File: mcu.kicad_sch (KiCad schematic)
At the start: 1 part, among them IC5 STM32G030K6T6

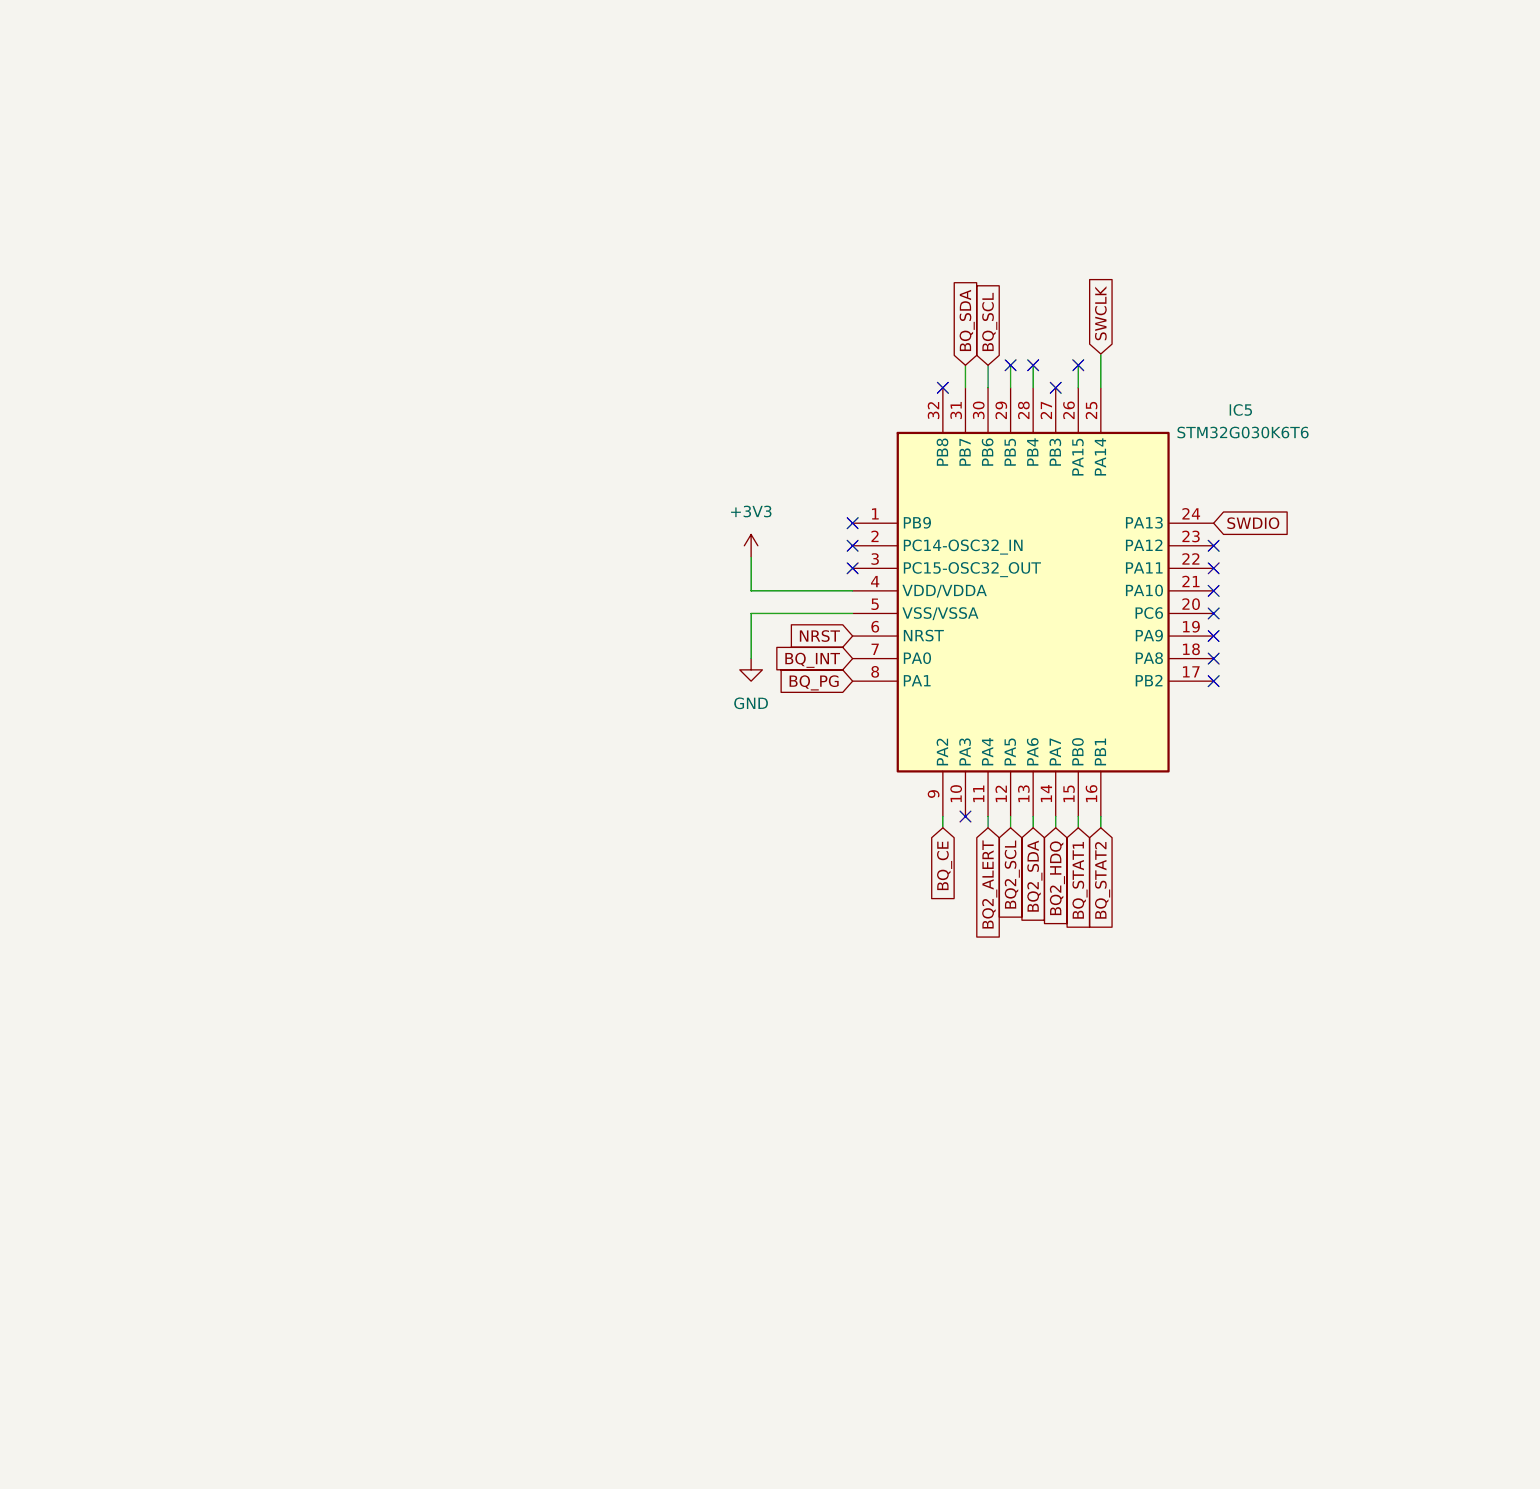
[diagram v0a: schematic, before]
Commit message: Added Canbus+LEDs+New STM32
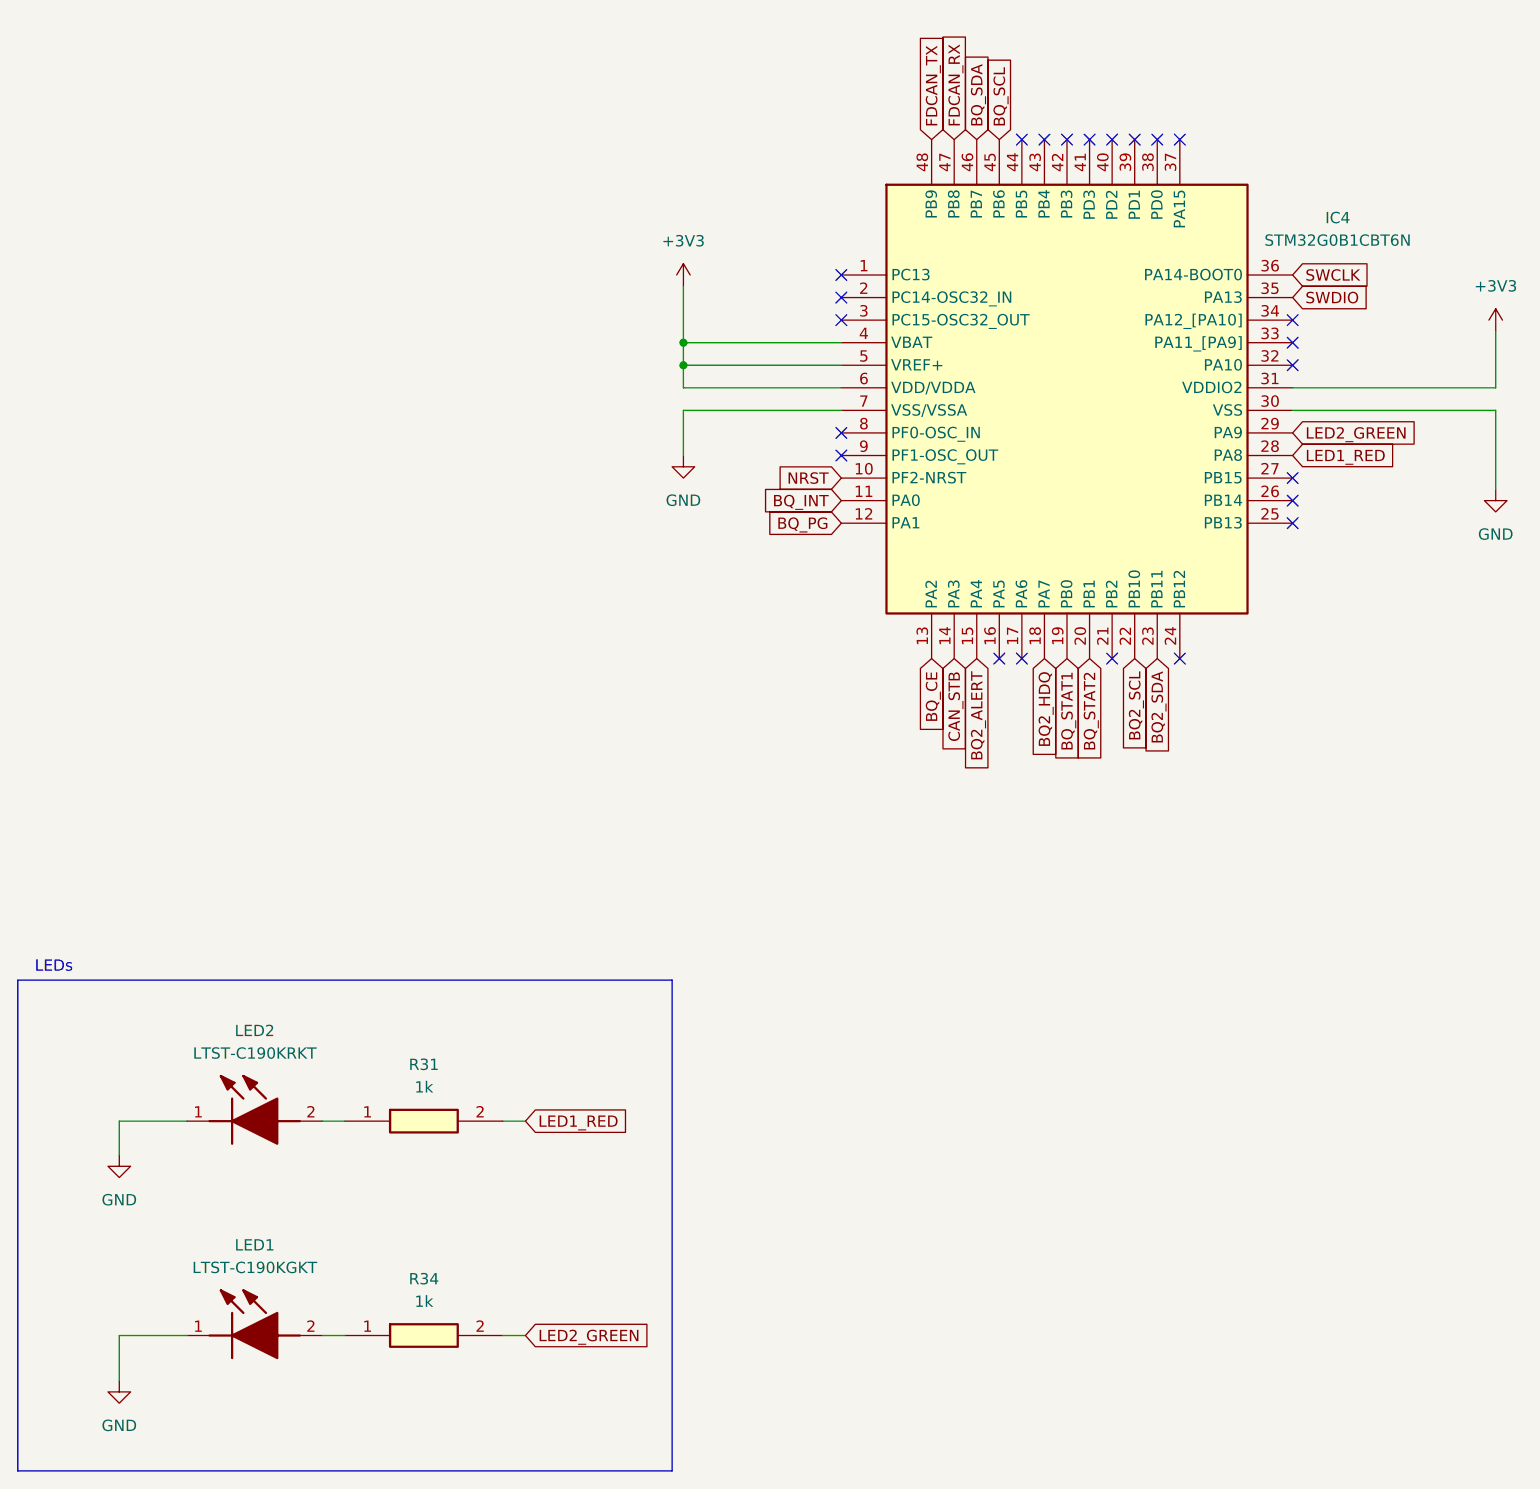
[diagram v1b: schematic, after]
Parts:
- removed IC5: STM32G030K6T6, STM32G030K6T6:QFP80P900X900X160-32N, symbol STM32G030K6T6:STM32G030K6T6
- added IC4: STM32G0B1CBT6N, STM32G0B1CBT6N:QFP50P900X900X160-48N, symbol STM32G0B1CBT6N:STM32G0B1CBT6N
- added LED1: LTST-C190KGKT, LTST-C190KGKT:LEDC1608X80N, symbol LTST-C190KGKT:LTST-C190KGKT
- added LED2: LTST-C190KRKT, LTST-C190KRKT:LEDC1608X80N, symbol LTST-C190KRKT:LTST-C190KRKT
- added R31, R34: 1k, RC0603FR-071KL:RESC1608X55N, symbol RC0603FR-071KL:RC0603FR-071KL
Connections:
- net +3V3: now also IC4.31 (VDDIO2), IC4.4 (VBAT), IC4.5 (VREF+), IC4.6 (VDD/VDDA)
- net BQ2_ALERT: now also IC4.15 (PA4)
- net BQ2_HDQ: now also IC4.18 (PA7)
- net BQ2_SCL: now also IC4.22 (PB10)
- net BQ2_SDA: now also IC4.23 (PB11)
- net BQ_CE: now also IC4.13 (PA2)
- net BQ_INT: now also IC4.11 (PA0)
- net BQ_PG: now also IC4.12 (PA1)
- net BQ_SCL: now also IC4.45 (PB6)
- net BQ_SDA: now also IC4.46 (PB7)
- net BQ_STAT1: now also IC4.19 (PB0)
- net BQ_STAT2: now also IC4.20 (PB1)
- net GND: now also IC4.30 (VSS), IC4.7 (VSS/VSSA), LED1.1 (K), LED2.1 (K)
- net NRST: now also IC4.10 (PF2-NRST)
- net SWCLK: now also IC4.36 (PA14-BOOT0)
- net SWDIO: now also IC4.35 (PA13)
- new net: LED2.2 (A), R31.1
- new net: LED1.2 (A), R34.1
- new net CAN_STB: IC4.14 (PA3)
- new net FDCAN_RX: IC4.47 (PB8)
- new net FDCAN_TX: IC4.48 (PB9)
- new net LED1_RED: IC4.28 (PA8), R31.2
- new net LED2_GREEN: IC4.29 (PA9), R34.2
- no-connect marks 16 -> 23
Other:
- note added: "LEDs"

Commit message: First Layout Try
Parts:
- added C14: 1uF, C2012X7R1H105K125AB:CAPC2012X145N, symbol C2012X7R1H105K125AB:C2012X7R1H105K125AB
- added C15, C27, C28: 0.1uF, CC0603KRX7R9BB104:CAPC1608X90N, symbol CC0603KRX7R9BB104:CC0603KRX7R9BB104
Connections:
- net +3V3: now also C14.1, C15.1, C27.1, C28.1
- net GND: now also C14.2, C15.2, C27.2, C28.2
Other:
- note added: "50V"
- note added: "Decoupling Capacitors"

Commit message: First Changes
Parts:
- removed C14: 1uF, C2012X7R1H105K125AB:CAPC2012X145N, symbol C2012X7R1H105K125AB:C2012X7R1H105K125AB
- added C14: 4.7uF, UMJ325AB7475KMHP:CAPC3225X280N, symbol UMJ325AB7475KMHP:UMJ325AB7475KMHP
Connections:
- net +3V3: now also C14.1
- net GND: now also C14.2
- net BQ2_SCLK: now reaches IC4.16 (PA5)
- net BQ2_MISO: now reaches IC4.17 (PA6)
- net BQ2_CS: now reaches IC4.24 (PB12)
- net BQ2_HDQ renamed BQ2_MOSI
- net BQ2_SCL: no longer names the net of IC4.22 (PB10)
- net BQ2_SDA: no longer names the net of IC4.23 (PB11)
- no-connect marks 23 -> 22
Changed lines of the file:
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@@
 	(text "50V"
 		(exclude_from_sim no)
-		(at 104.14 161.544 0)
+		(at 103.378 161.798 0)
 		(effects
 			(font
@@
 	)
 	(no_connect
-		(at 137.16 97.79)
+		(at 152.4 97.79)
 	)
 	(no_connect
@@
 	)
 	(no_connect
-		(at 134.62 97.79)
-	)
-	(no_connect
 		(at 149.86 39.37)
-	)
-	(no_connect
-		(at 154.94 97.79)
 	)
 	(no_connect
@@
 	(no_connect
 		(at 167.64 82.55)
+	)
+	(no_connect
+		(at 149.86 97.79)
 	)
 	(no_connect
@@
 		)
 	)
-	(global_label "BQ2_HDQ"
+	(global_label "BQ2_MOSI"
 		(shape input)
 		(at 139.7 97.79 270)
@@
 		)
 		(property "Intersheetrefs" "${INTERSHEET_REFS}"
-			(at 139.7 109.4838 90)
+			(at 139.7 110.149 90)
 			(effects
 				(font
@@
 		)
 	)
+	(global_label "BQ2_CS"
+		(shape input)
+		(at 154.94 97.79 270)
+		(fields_autoplaced yes)
+		(effects
+			(font
+				(size 1.27 1.27)
+			)
+			(justify right)
+		)
+		(property "Intersheetrefs" "${INTERSHEET_REFS}"
+			(at 154.94 108.0323 90)
+			(effects
+				(font
+					(size 1.27 1.27)
+				)
+				(justify right)
+				(hide yes)
+			)
+		)
+	)
 	(global_label "LED1_RED"
 		(shape input)
@@
 		)
 	)
+	(global_label "BQ2_SCLK"
+		(shape input)
+		(at 134.62 97.79 270)
+		(fields_autoplaced yes)
+		(effects
+			(font
+				(size 1.27 1.27)
+			)
+			(justify right)
+		)
+		(property "Intersheetrefs" "${INTERSHEET_REFS}"
+			(at 134.62 110.3304 90)
+			(effects
+				(font
+					(size 1.27 1.27)
+				)
+				(justify right)
+				(hide yes)
+			)
+		)
+	)
 	(global_label "SWCLK"
 		(shape input)
@@
 		)
 	)
-	(global_label "BQ2_SDA"
-		(shape input)
-		(at 152.4 97.79 270)
-		(fields_autoplaced yes)
-		(effects
-			(font
-				(size 1.27 1.27)
-			)
-			(justify right)
-		)
-		(property "Intersheetrefs" "${INTERSHEET_REFS}"
-			(at 152.4 109.1209 90)
-			(effects
-				(font
-					(size 1.27 1.27)
-				)
-				(justify right)
-				(hide yes)
-			)
-		)
-	)
 	(global_label "BQ_STAT2"
 		(shape input)
@@
 		)
 	)
-	(global_label "BQ2_SCL"
-		(shape input)
-		(at 149.86 97.79 270)
-		(fields_autoplaced yes)
-		(effects
-			(font
-				(size 1.27 1.27)
-			)
-			(justify right)
-		)
-		(property "Intersheetrefs" "${INTERSHEET_REFS}"
-			(at 149.86 109.0604 90)
-			(effects
-				(font
-					(size 1.27 1.27)
-				)
-				(justify right)
-				(hide yes)
-			)
-		)
-	)
 	(global_label "BQ_INT"
 		(shape input)
@@
 		(property "Intersheetrefs" "${INTERSHEET_REFS}"
 			(at 107.3838 80.01 0)
+			(effects
+				(font
+					(size 1.27 1.27)
+				)
+				(justify right)
+				(hide yes)
+			)
+		)
+	)
+	(global_label "BQ2_MISO"
+		(shape input)
+		(at 137.16 97.79 270)
+		(fields_autoplaced yes)
+		(effects
+			(font
+				(size 1.27 1.27)
+			)
+			(justify right)
+		)
+		(property "Intersheetrefs" "${INTERSHEET_REFS}"
+			(at 137.16 110.149 90)
 			(effects
 				(font
@@
 	)
 	(symbol
-		(lib_id "C2012X7R1H105K125AB:C2012X7R1H105K125AB")
-		(at 110.49 154.94 270)
-		(unit 1)
-		(exclude_from_sim no)
-		(in_bom yes)
-		(on_board yes)
-		(dnp no)
-		(fields_autoplaced yes)
-		(property "Reference" "C14"
-			(at 114.3 160.0199 90)
-			(effects
-				(font
-					(size 1.27 1.27)
-				)
-				(justify left)
-			)
-		)
-		(property "Value" "1uF"
-			(at 114.3 162.5599 90)
-			(effects
-				(font
-					(size 1.27 1.27)
-				)
-				(justify left)
-			)
-		)
-		(property "Footprint" "C2012X7R1H105K125AB:CAPC2012X145N"
-			(at 14.3 163.83 0)
-			(effects
-				(font
-					(size 1.27 1.27)
-				)
-				(justify left top)
-				(hide yes)
-			)
-		)
-		(property "Datasheet" "https://product.tdk.com/info/en/catalog/datasheets/mlcc_commercial_midvoltage_en.pdf"
-			(at -85.7 163.83 0)
-			(effects
-				(font
-					(size 1.27 1.27)
-				)
-				(justify left top)
-				(hide yes)
-			)
-		)
-		(property "Description" "MULTILAYER CERAMIC CHIP CAPACITORS, 2012, Commercial grade, general (Up to 75V)"
-			(at 110.49 154.94 0)
-			(effects
-				(font
-					(size 1.27 1.27)
-				)
-				(hide yes)
-			)
-		)
-		(property "Height" "1.45"
-			(at -285.7 163.83 0)
-			(effects
-				(font
-					(size 1.27 1.27)
-				)
-				(justify left top)
-				(hide yes)
-			)
-		)
-		(property "Mouser Part Number" "810-C2012X7R1H105K"
-			(at -385.7 163.83 0)
-			(effects
-				(font
-					(size 1.27 1.27)
-				)
-				(justify left top)
-				(hide yes)
-			)
-		)
-		(property "Mouser Price/Stock" "https://www.mouser.co.uk/ProductDetail/TDK/C2012X7R1H105K125AB?qs=NRhsANhppD9AlYlb8kBg7Q%3D%3D"
-			(at -485.7 163.83 0)
-			(effects
-				(font
-					(size 1.27 1.27)
-				)
-				(justify left top)
-				(hide yes)
-			)
-		)
-		(property "Manufacturer_Name" "TDK"
-			(at -585.7 163.83 0)
-			(effects
-				(font
-					(size 1.27 1.27)
-				)
-				(justify left top)
-				(hide yes)
-			)
-		)
-		(property "Manufacturer_Part_Number" "C2012X7R1H105K125AB"
-			(at -685.7 163.83 0)
-			(effects
-				(font
-					(size 1.27 1.27)
-				)
-				(justify left top)
-				(hide yes)
-			)
-		)
-		(pin "1"
-		)
-		(pin "2"
-		)
-		(instances
-			(project "Lithium_Board"
-				(path "/a208389b-7ee7-48d8-95f2-b3e129849547/160492a7-828d-4540-9766-a6c613c08096"
-					(reference "C14")
-					(unit 1)
-				)
-			)
-		)
-	)
-	(symbol
 		(lib_id "power:+3V3")
 		(at 124.46 152.4 0)
@@
 					(unit 1)
 				)
+			)
+		)
+	)
+	(symbol
+		(lib_id "UMJ325AB7475KMHP:UMJ325AB7475KMHP")
+		(at 110.49 154.94 270)
+		(unit 1)
+		(exclude_from_sim no)
+		(in_bom yes)
+		(on_board yes)
+		(dnp no)
+		(fields_autoplaced yes)
+		(property "Reference" "C14"
+			(at 114.3 160.0199 90)
+			(effects
+				(font
+					(size 1.27 1.27)
+				)
+				(justify left)
+			)
+		)
+		(property "Value" "4.7uF"
+			(at 114.3 162.5599 90)
+			(effects
+				(font
+					(size 1.27 1.27)
+				)
+				(justify left)
+			)
+		)
+		(property "Footprint" "UMJ325AB7475KMHP:CAPC3225X280N"
+			(at 14.3 163.83 0)
+			(effects
+				(font
+					(size 1.27 1.27)
+				)
+				(justify left top)
+				(hide yes)
+			)
+		)
+		(property "Datasheet" "https://ds.yuden.co.jp/TYCOMPAS/or/specSheet?pn=MCJCU32MAB7475KPPA01"
+			(at -85.7 163.83 0)
+			(effects
+				(font
+					(size 1.27 1.27)
+				)
+				(justify left top)
+				(hide yes)
+			)
+		)
+		(property "Description" "4.7 F +/-10% 50V Ceramic Capacitor X7R 1210 (3225 Metric)"
+			(at 110.49 154.94 0)
+			(effects
+				(font
+					(size 1.27 1.27)
+				)
+				(hide yes)
+			)
+		)
+		(property "Height" "2.8"
+			(at -285.7 163.83 0)
+			(effects
+				(font
+					(size 1.27 1.27)
+				)
+				(justify left top)
+				(hide yes)
+			)
+		)
+		(property "Mouser Part Number" "963-UMJ325AB7475KMHP"
+			(at -385.7 163.83 0)
+			(effects
+				(font
+					(size 1.27 1.27)
+				)
+				(justify left top)
+				(hide yes)
+			)
+		)
+		(property "Mouser Price/Stock" "https://www.mouser.co.uk/ProductDetail/TAIYO-YUDEN/UMJ325AB7475KMHP?qs=sBf%2Fb4nBSlehnKp%252BnIaW0Q%3D%3D"
+			(at -485.7 163.83 0)
+			(effects
+				(font
+					(size 1.27 1.27)
+				)
+				(justify left top)
+				(hide yes)
+			)
+		)
+		(property "Manufacturer_Name" "TAIYO YUDEN"
+			(at -585.7 163.83 0)
+			(effects
+				(font
+					(size 1.27 1.27)
+				)
+				(justify left top)
+				(hide yes)
+			)
+		)
+		(property "Manufacturer_Part_Number" "UMJ325AB7475KMHP"
+			(at -685.7 163.83 0)
+			(effects
+				(font
+					(size 1.27 1.27)
+				)
+				(justify left top)
+				(hide yes)
+			)
+		)
+		(pin "2"
+		)
+		(pin "1"
+		)
+		(instances
+			(project "Lithium_Board"
+				(path "/a208389b-7ee7-48d8-95f2-b3e129849547/160492a7-828d-4540-9766-a6c613c08096"
+					(reference "C14")
+					(unit 1)
+				)
